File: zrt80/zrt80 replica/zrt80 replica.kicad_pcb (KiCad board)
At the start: 2 copper layers, 228.6 x 165.7 mm, 108 parts, among them J1 VIDEO, J2 POWER, J3 KEYBOARD, J4 S2-S3, J5 RS232, J6 CHAR, J7 RAM, Q1 2N2222, Q2 2N5484, Y1 20MHz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

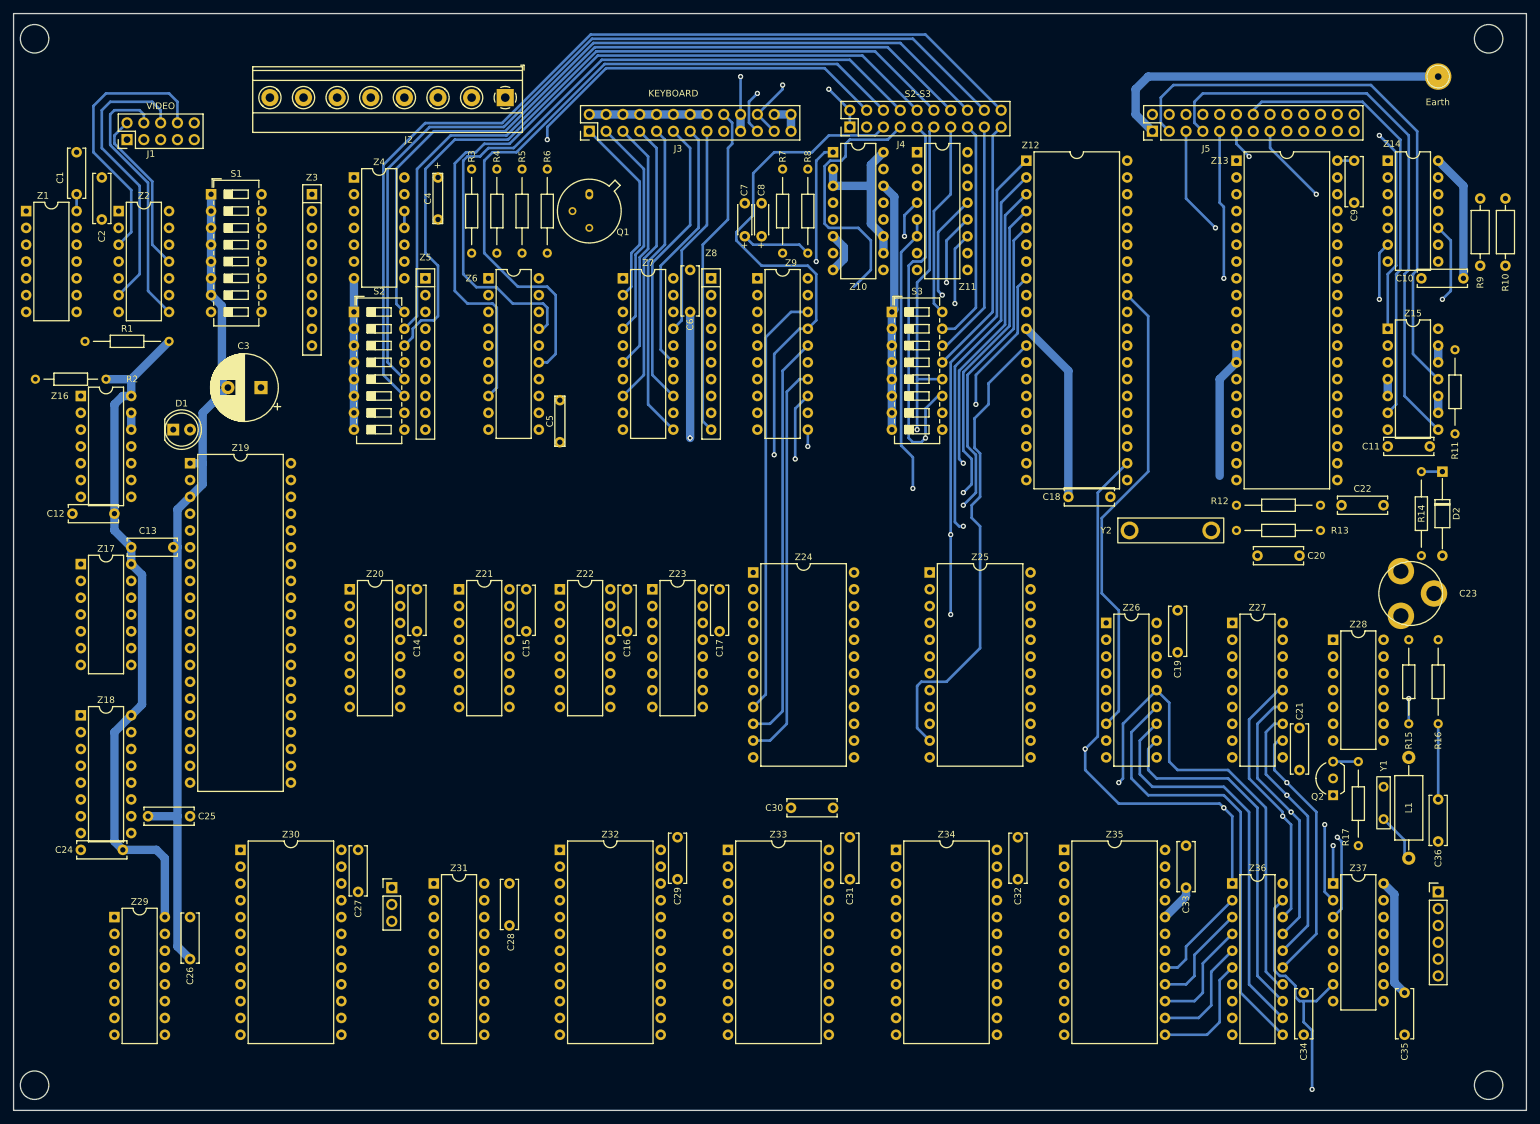
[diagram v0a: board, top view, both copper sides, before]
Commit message: continued zrt80 layout
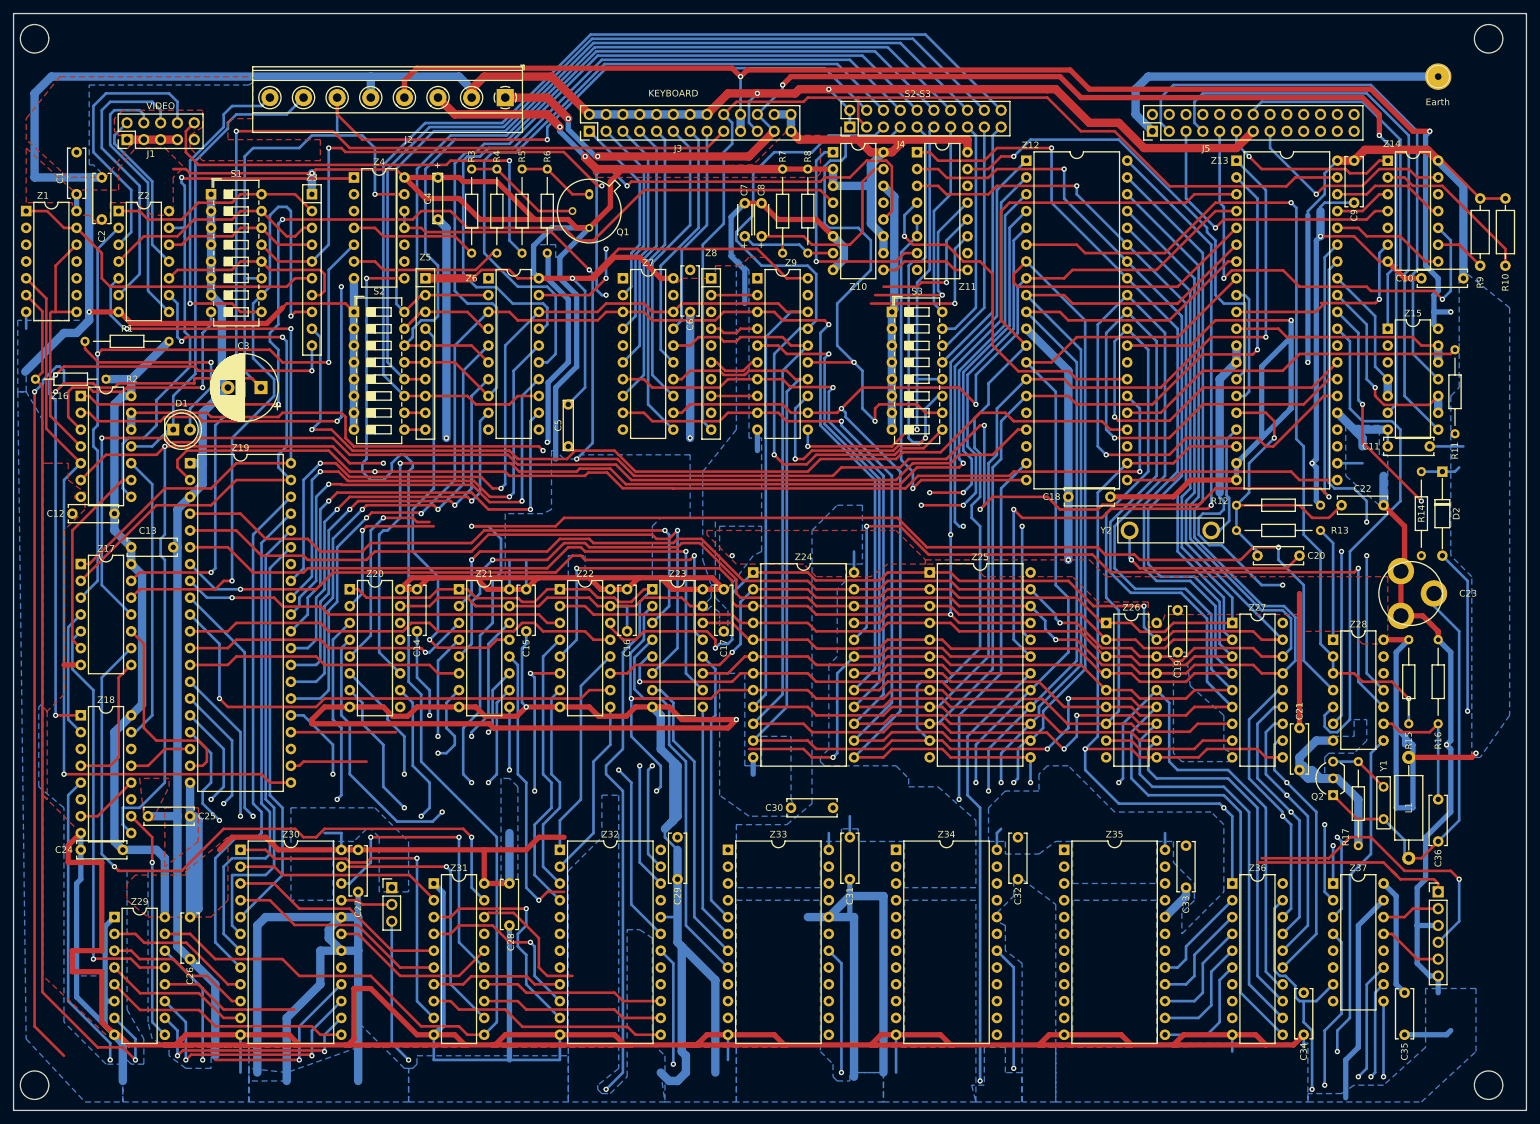
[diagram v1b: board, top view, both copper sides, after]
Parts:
- moved C5 1.42 mm to (98.4, 82.5)
- moved C17 0.64 mm to (121.9, 110.5)
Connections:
- Q2 pad 1: GND -> Net-(C23-Pad1)
- Q2 pad 2: Net-(C23-Pad1) -> GND
- R2 pad 1: Net-(Z1-Cp1) -> DOT CLK
- R9 pad 1: Net-(Z14-RESPONSE_COTROL_D) -> Net-(Z14-RESPONSE_COTROL_C)
- Z1 pad 6: Net-(Z1-Cp1) -> DOT CLK
- Z14 pad 12: Net-(Z14-RESPONSE_COTROL_D) -> unconnected-(Z14-RESPONSE_COTROL_D-Pad12)
- Z14 pad 9: unconnected-(Z14-RESPONSE_COTROL_C-Pad9) -> Net-(Z14-RESPONSE_COTROL_C)
- Z19 pad 2: /reset -> /RESET
- Z26 pad 5: A0 -> A2
- Z26 pad 7: A2 -> A0
- Z27 pad 5: A0 -> A2
- Z27 pad 7: A2 -> A0
- Z28 pad 8: Net-(Z1-Cp1) -> DOT CLK
- Z5 pad 2: SW2-2 -> SW2-1
- Z9 pad 10: unconnected-(Z9-GND-Pad10) -> GND
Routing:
- net GND: track 250.9 -> 2014.4 mm, vias 3 -> 13
- net +5V: track 228.9 -> 996.1 mm, vias 0 -> 9
- net D7: track 39.9 -> 369.4 mm, vias 1 -> 5
- net D0: track 119.2 -> 428.3 mm, vias 0 -> 3
- net D4: track 39.9 -> 346.0 mm, vias 1 -> 5
- net D5: track 40.3 -> 342.9 mm, vias 1 -> 5
- net D6: track 40.3 -> 327.6 mm, vias 1 -> 5
- net D1: track 122.8 -> 409.6 mm, vias 0 -> 5
- net EXRESET: track 56.5 -> 340.7 mm, vias 1 -> 5
- net A0: track 0.00 -> 259.7 mm, vias 0 -> 3
- net D3: track 95.7 -> 341.1 mm, vias 2 -> 6
- net A9: track 0.00 -> 239.1 mm, vias 0 -> 2
- net RESET: track 2.54 -> 236.9 mm, vias 0 -> 5
- net A1: track 0.00 -> 234.0 mm, vias 0 -> 2
- net A5: track 0.00 -> 226.4 mm, vias 0 -> 2
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- added copper zone on B.Cu, net +5V
- added copper zone on F.Cu, net +5V
- added copper zone on B.Cu, net GND
- added copper zone on F.Cu, net GND

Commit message: finished initial layout of zrt-80
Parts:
- added G***: LOGO, Evan's parts:pcbway logo, B.Cu at (168.9, 29.8)
- added G***: LOGO, Evan's parts:Evan Logo, B.Cu at (83.2, 26.7)
- added G***: LOGO, Evan's parts:OSHW gear, B.Cu at (237.5, 39.4)
- moved C5 1.91 mm to (98.4, 80.6)
- moved C33 0.64 mm to (191.8, 149.9)
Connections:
- Z11 pad 4: ~{M1} -> ~{IO REQ}
- Z11 pad 6: ~{IO REQ} -> ~{M1}
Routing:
- net GND: track 2014.4 -> 2542.5 mm, vias 13 -> 14
- net +5V: track 996.1 -> 1372.4 mm
- net EXRESET: track 340.7 -> 612.0 mm
- net CA11: track 55.8 -> 299.8 mm, vias 3 -> 4
- net DOT CLK: track 183.1 -> 367.2 mm
- net /mem3: track 213.7 -> 395.9 mm
- net I/O1: track 12.6 -> 193.6 mm, vias 1 -> 3
- net A12: track 127.4 -> 274.8 mm
- net /WR: track 164.5 -> 301.0 mm
- net Net-(Z13-~{OUT1}): track 113.5 -> 248.9 mm, vias 2 -> 3
- net RAM A12: track 65.8 -> 199.1 mm
- net RAM A11: track 69.7 -> 195.2 mm
- net RAM A8: track 32.2 -> 147.6 mm
- net RAM A9: track 31.7 -> 144.9 mm
- net A15: track 66.1 -> 179.2 mm, vias 3 -> 4
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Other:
- board text added: "$0000 - $0FFF mirrored $2000 - $2FFF"
- board text added: "$1000 - $1FFF mirrored $3000 - $3FFF"
- board text added: "$4000 - $43FF mirrored in chunks up to $7C00 - $7FFF"
- board text added: "$C000 - $CFFF"
- board text added: "$D000 - $DFFF"
- board text added: "$E000 - $EFFF"
- board text added: "$F000 - $FFFF"
- board text added: "+12"
- board text added: "+12v"
- board text added: "+5"
- board text added: "+5v"
- board text added: "-12"
- board text added: "-12v"
- board text added: "00 - odd 10 - even 01 - mark 11 - space"
- board text added: "0000 - 50 1000 - 75 0100 - 110 1100 - 134.5 0010 - 150 1010 - 300"
- board text added: "0011 - 4800 1011 - 7200 0111 - 9600 1111 - 19,200"
- board text added: "0110 - 600 1110 - 1200 0001 - 1800 1001 - 2000 0101 - 2400 1101 - 3600"
- board text added: "1"
- board text added: "1234"
- board text added: "18/4"
- board text added: "2"
- board text added: "2716"
- board text added: "2732"
- board text added: "3"
- board text added: "4"
- board text added: "5"
- board text added: "56"
- board text added: "6"
- board text added: "ALT"
- board text added: "AUTO LF"
- board text added: "BAUD RATE"
- board text added: "BEEP"
- board text added: "BPR"
- board text added: "Bit 0"
- board text added: "Bit 1"
- board text added: "Bit 2"
- board text added: "Bit 3"
- board text added: "Bit 4"
- board text added: "Bit 5"
- board text added: "Bit 6"
- board text added: "CD"
- board text added: "COPYRIGHT 1983 WILLIAM WHITE AND DIGITAL RESEARCH COMPUTERS"
- board text added: "CSYN"
- board text added: "CTS"
- board text added: "Csync"
- board text added: "DSR"
- board text added: "DTR"
- board text added: "GND"
- board text added: "HSYN"
- board text added: "Hsync"
- board text added: "KSTB"
- board text added: "LCL CPY"
- board text added: "LED"
- board text added: "LOCAL"
- board text added: "PARITY"
- board text added: "PCB-1"
- board text added: "RES"
- board text added: "RESET"
- board text added: "RS-232"
- board text added: "RTS"
- board text added: "Rx"
- board text added: "SW2-1"
- board text added: "SW2-2"
- board text added: "SW2-3"
- board text added: "SW2-4"
- board text added: "SW2-5"
- board text added: "SW2-6"
- board text added: "SW2-7"
- board text added: "SW2-8"
- board text added: "Strobe"
- board text added: "TERMINAL"
- board text added: "Tx"
- board text added: "VIDEO"
- board text added: "VSYN"
- board text added: "Vsync"
- board text added: "WRAP"
- board text added: "X=CTL"
- board text added: "ZRT-80 reproduction"
- board text added: "abzman2k.wordpress.com"
- board text added: "alternate keypad"
- board text added: "caps lock"
- board text added: "char. rom size"
- board text added: "comp. vid."
- board text added: "earth"
- board text added: "populate always"
- board text added: "populate for 2+ chip configs"
- board text added: "populate for 4 chip config"
- board text added: "ram chips"
- board text added: "sw3-1"
- board text added: "sw3-2"
- board text added: "sw3-3"
- board text added: "sw3-4"
- board text added: "sw3-5"
- board text added: "sw3-6"
- board text added: "sw3-7"
- board text added: "sw3-8"
- board text added: "video"

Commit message: updated silk and added note for doubling the rom
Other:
- board text added: "2114"
- board text added: "2716 or 2732"
- board text added: "6116"
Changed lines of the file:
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@@
+    (effects (font (size 1 1) (thickness 0.15)) (justify left bottom mirror))
+  )
+  (gr_text "2114" (at 185.42 123.825) (layer "B.SilkS")
     (effects (font (size 1 1) (thickness 0.15)) (justify left bottom mirror))
   )
@@
     (effects (font (size 1 1) (thickness 0.15)) (justify left bottom mirror))
   )
+  (gr_text "6116" (at 107.315 147.32) (layer "B.SilkS")
+    (effects (font (size 1 1) (thickness 0.15)) (justify left bottom mirror))
+  )
   (gr_text "SW2-4" (at 151.765 31.75 90) (layer "B.SilkS")
     (effects (font (size 1 1) (thickness 0.15)) (justify left bottom mirror))
@@
     (effects (font (size 1 1) (thickness 0.15)) (justify left bottom mirror))
   )
+  (gr_text "2732" (at 162.56 108.585) (layer "B.SilkS")
+    (effects (font (size 1 1) (thickness 0.15)) (justify left bottom mirror))
+  )
   (gr_text "sw3-5" (at 155.575 41.91 90) (layer "B.SilkS")
     (effects (font (size 1 1) (thickness 0.15)) (justify left bottom mirror))
@@
     (effects (font (size 1 1) (thickness 0.15)) (justify left bottom mirror))
   )
+  (gr_text "2732" (at 135.89 108.585) (layer "B.SilkS")
+    (effects (font (size 1 1) (thickness 0.15)) (justify left bottom mirror))
+  )
   (gr_text "+5v" (at 132.715 34.29 90) (layer "B.SilkS")
     (effects (font (size 1 1) (thickness 0.15)) (justify left bottom mirror))
@@
     (effects (font (size 1 1) (thickness 0.15)) (justify left bottom mirror))
   )
+  (gr_text "6116" (at 182.245 147.32) (layer "B.SilkS")
+    (effects (font (size 1 1) (thickness 0.15)) (justify left bottom mirror))
+  )
   (gr_text "+5v" (at 132.715 42.545 90) (layer "B.SilkS")
     (effects (font (size 1 1) (thickness 0.15)) (justify left bottom mirror))
@@
     (effects (font (size 1 1) (thickness 0.15)) (justify left bottom mirror))
   )
+  (gr_text "6116" (at 156.845 147.32) (layer "B.SilkS")
+    (effects (font (size 1 1) (thickness 0.15)) (justify left bottom mirror))
+  )
   (gr_text "Csync" (at 40.005 34.29 90) (layer "B.SilkS")
     (effects (font (size 1 1) (thickness 0.15)) (justify left bottom mirror))
@@
     (effects (font (size 1 1) (thickness 0.15)) (justify left bottom mirror))
   )
+  (gr_text "6116" (at 132.08 147.32) (layer "B.SilkS")
+    (effects (font (size 1 1) (thickness 0.15)) (justify left bottom mirror))
+  )
   (gr_text "1" (at 234.315 170.815) (layer "B.SilkS")
     (effects (font (size 1 1) (thickness 0.15)) (justify left bottom mirror))
@@
     (effects (font (size 1 1) (thickness 0.15)) (justify left bottom mirror))
   )
+  (gr_text "2114" (at 204.47 123.825) (layer "B.SilkS")
+    (effects (font (size 1 1) (thickness 0.15)) (justify left bottom mirror))
+  )
   (gr_text "populate for\n2+ chip\nconfigs" (at 160.02 154.305) (layer "B.SilkS")
     (effects (font (size 1 1) (thickness 0.15)) (justify left bottom mirror))
@@
     (effects (font (size 1 1) (thickness 0.15)) (justify left bottom mirror))
   )
+  (gr_text "2716 or 2732" (at 62.23 150.495) (layer "B.SilkS")
+    (effects (font (size 1 1) (thickness 0.15)) (justify left bottom mirror))
+  )
